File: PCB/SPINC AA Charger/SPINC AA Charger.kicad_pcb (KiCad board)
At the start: 4 copper layers, 70 x 72 mm, 84 parts, among them J1 USB_C_Receptacle_USB2.0, J2 Conn_01x03_Pin, J3 Conn_01x10_Socket, J4 Conn_01x01_Pin, J5 Conn_01x01_Pin, Q1 DMG2301L, Q2 DMHC3025LSD, Q3 DMG2301L, Q4 DMG2301L, Q5 SI2305CDS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

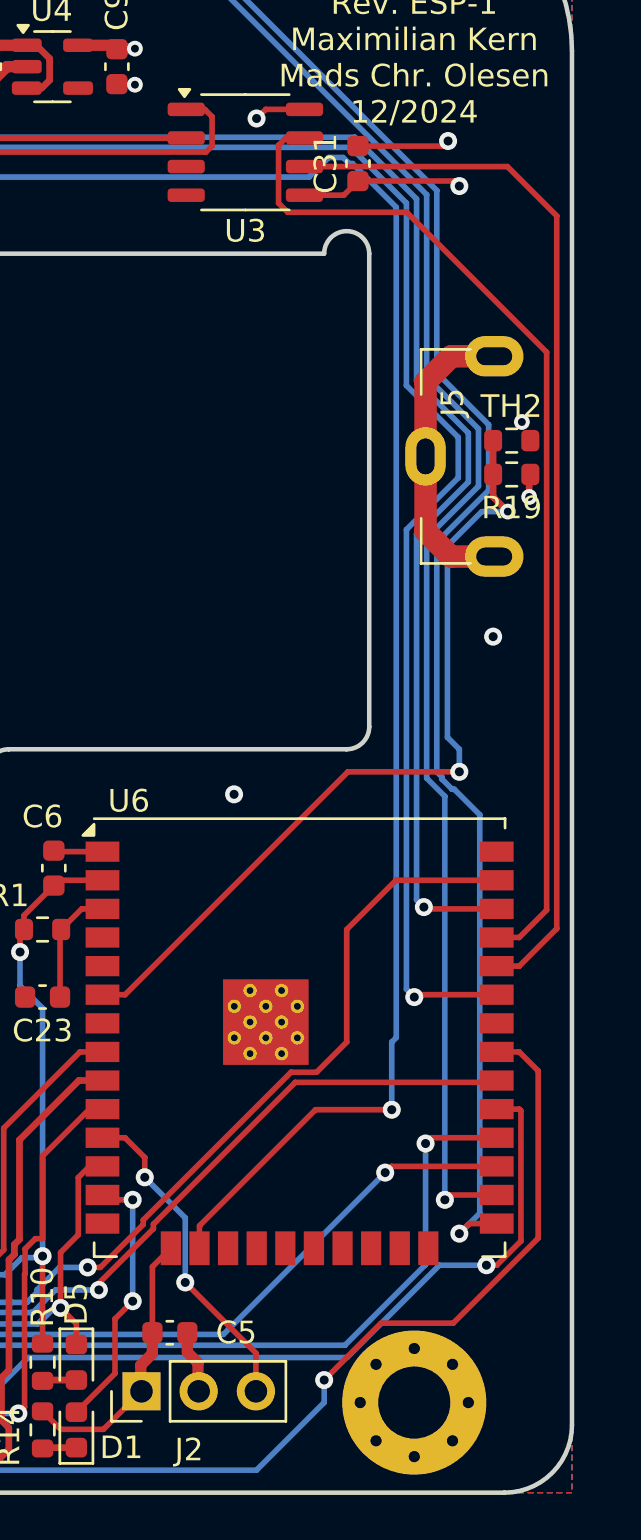
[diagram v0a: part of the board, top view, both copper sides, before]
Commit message: Fix a few routing warnings
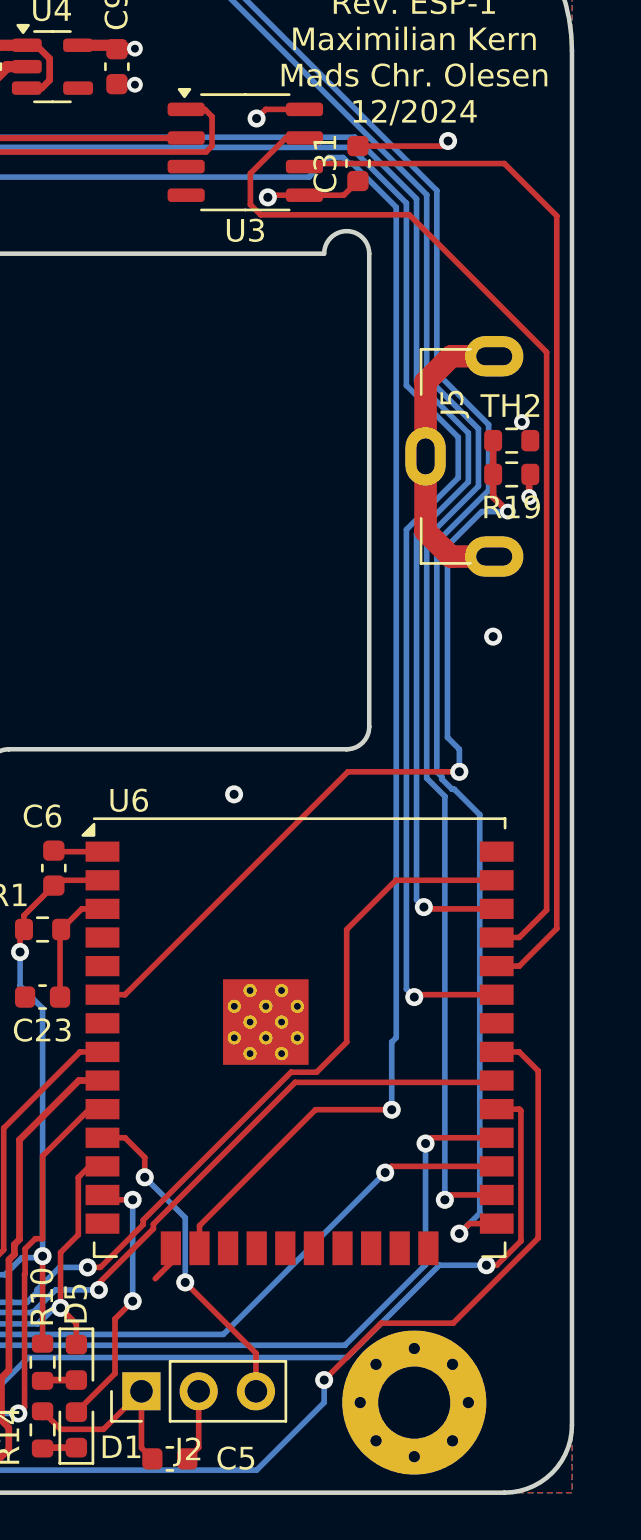
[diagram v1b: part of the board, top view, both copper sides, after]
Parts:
- moved C5 5.60 mm to (167.2, 134.5)
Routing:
- net GND: track 38.5 -> 36.4 mm
- net TX: track 46.0 -> 47.8 mm
- net +3V3: track 9.66 -> 10.4 mm
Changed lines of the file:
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@@
 	(title_block
 		(title "SPINC AA Charger")
-		(date "2024-09-29")
-		(rev "2")
-		(company "Maximilian Kern")
+		(date "2024-12-14")
+		(rev "ESP-1")
+		(company "Maximilian Kern, Mads Chr. Olesen")
 	)
 	(layers
@@
 	(footprint "Capacitor_SMD:C_0603_1608Metric"
 		(layer "F.Cu")
-		(at 167.15 128.9 180)
+		(at 167.15 134.5 180)
 		(descr "Capacitor SMD 0603 (1608 Metric), square (rectangular) end terminal, IPC_7351 nominal, (Body size source: IPC-SM-782 page 76, https://www.pcb-3d.com/wordpress/wp-content/uploads/ipc-sm-782a_amendment_1_and_2.pdf), generated with kicad-footprint-generator")
 		(tags "capacitor")
@@
 	)
 	(segment
-		(start 166.375 128.9)
-		(end 166.375 125.97)
-		(width 0.25)
-		(layer "F.Cu")
-		(net 5)
-	)
-	(segment
-		(start 166.375 129)
-		(end 166.375 129.825)
-		(width 0.5)
-		(layer "F.Cu")
-		(net 5)
-	)
-	(segment
-		(start 165.86 130.34)
-		(end 165.86 131.6)
-		(width 0.5)
-		(layer "F.Cu")
-		(net 5)
-	)
-	(segment
 		(start 179.275 76.225)
 		(end 179.5 76)
@@
 	)
 	(segment
+		(start 165.89 134.015)
+		(end 166.375 134.5)
+		(width 0.25)
+		(layer "F.Cu")
+		(net 5)
+	)
+	(segment
 		(start 161.5 132.3875)
 		(end 162.3 133.1875)
@@
 	)
 	(segment
-		(start 166.375 125.97)
-		(end 167.195 125.15)
-		(width 0.25)
-		(layer "F.Cu")
-		(net 5)
-	)
-	(segment
-		(start 166.375 129.825)
-		(end 165.86 130.34)
-		(width 0.5)
-		(layer "F.Cu")
-		(net 5)
-	)
-	(segment
 		(start 148.75 69.91)
 		(end 149.46 69.2)
@@
 	)
 	(segment
+		(start 167.195 125.15)
+		(end 167.195 125.805)
+		(width 0.25)
+		(layer "F.Cu")
+		(net 5)
+	)
+	(segment
 		(start 149.46 69.2)
 		(end 151.04 69.2)
@@
 	)
 	(segment
+		(start 165.89 131.5)
+		(end 165.89 134.015)
+		(width 0.25)
+		(layer "F.Cu")
+		(net 5)
+	)
+	(segment
 		(start 150.4 73.475)
 		(end 150.4 74.045405)
@@
 	)
 	(segment
+		(start 167.195 125.805)
+		(end 166.5 126.5)
+		(width 0.25)
+		(layer "F.Cu")
+		(net 5)
+	)
+	(segment
 		(start 175.5 76.225)
 		(end 179.275 76.225)
@@
 	)
 	(segment
+		(start 168.43 131.5)
+		(end 168.43 133.995)
+		(width 0.25)
+		(layer "F.Cu")
+		(net 24)
+	)
+	(segment
 		(start 161.8125 73.299999)
 		(end 161.8125 72.338738)
@@
 	)
 	(segment
+		(start 168.43 133.995)
+		(end 167.925 134.5)
+		(width 0.25)
+		(layer "F.Cu")
+		(net 24)
+	)
+	(segment
 		(start 142.9 69.4125)
 		(end 139.6 69.4125)
@@
 	)
 	(segment
-		(start 167.925 129.7625)
-		(end 168.4 130.2375)
-		(width 0.5)
-		(layer "F.Cu")
-		(net 24)
-	)
-	(segment
 		(start 133.7 69.4125)
 		(end 127.3875 69.4125)
@@
 	)
 	(segment
-		(start 167.925 129)
-		(end 167.925 129.7625)
-		(width 0.5)
-		(layer "F.Cu")
-		(net 24)
-	)
-	(segment
 		(start 161.223762 71.75)
 		(end 160.8 71.75)
@@
 	)
 	(segment
-		(start 168.4 130.2375)
-		(end 168.4 131.6)
-		(width 0.5)
-		(layer "F.Cu")
-		(net 24)
-	)
-	(segment
 		(start 126.2075 72.94)
 		(end 126.2075 71.9075)
@@
 	)
 	(segment
-		(start 175.5 77.775)
-		(end 179.775 77.775)
+		(start 171.595 78.405)
+		(end 171.5 78.5)
 		(width 0.25)
 		(layer "F.Cu")
@@
 	)
 	(segment
-		(start 171.405 74.595)
-		(end 171 75)
+		(start 173.125 78.405)
+		(end 171.595 78.405)
 		(width 0.25)
 		(layer "F.Cu")
@@
 	)
 	(segment
-		(start 173.22 78.5)
-		(end 173.125 78.405)
+		(start 171.405 74.595)
+		(end 171 75)
 		(width 0.25)
 		(layer "F.Cu")
@@
 	)
 	(segment
-		(start 179.775 77.775)
-		(end 180 78)
+		(start 173.22 78.5)
+		(end 173.125 78.405)
 		(width 0.25)
 		(layer "F.Cu")
@@
 	)
 	(via
-		(at 180 78)
+		(at 171.5 78.5)
 		(size 0.8)
 		(drill 0.4)
@@
 	)
 	(segment
-		(start 171.975 78.755908)
-		(end 172.381031 79.161939)
+		(start 171 78)
+		(end 171.5 78.5)
 		(width 0.25)
-		(layer "F.Cu")
-		(net 76)
+		(layer "In2.Cu")
+		(net 74)
 	)
 	(segment
-		(start 172.381031 79.161939)
-		(end 177.661939 79.161939)
+		(start 171 75)
+		(end 171 78)
+		(width 0.25)
+		(layer "In2.Cu")
+		(net 74)
+	)
+	(segment
+		(start 182.66 111.355)
+		(end 181.66 111.355)
 		(width 0.25)
 		(layer "F.Cu")
@@
 	)
 	(segment
-		(start 172.300001 75.865)
-		(end 171.975 76.190001)
+		(start 183.875 85.375)
+		(end 183.875 110.14)
 		(width 0.25)
 		(layer "F.Cu")
@@
 	)
 	(segment
-		(start 182.66 111.355)
-		(end 181.66 111.355)
+		(start 171.178984 79.275)
+		(end 177.775 79.275)
 		(width 0.25)
 		(layer "F.Cu")
@@
 	)
 	(segment
-		(start 183.875 85.375)
-		(end 183.875 110.14)
+		(start 172.300001 75.865)
+		(end 170.725 77.440001)
 		(width 0.25)
 		(layer "F.Cu")
@@
 	)
 	(segment
-		(start 171.975 76.190001)
-		(end 171.975 78.755908)
+		(start 177.775 79.275)
+		(end 183.875 85.375)
 		(width 0.25)
 		(layer "F.Cu")
@@
 	)
 	(segment
-		(start 177.661939 79.161939)
-		(end 183.875 85.375)
+		(start 170.725 78.821016)
+		(end 171.178984 79.275)
 		(width 0.25)
 		(layer "F.Cu")
@@
 	)
 	(segment
-		(start 184.325 79.325)
-		(end 184.325 110.96)
+		(start 170.725 77.440001)
+		(end 170.725 78.821016)
+		(width 0.25)
+		(layer "F.Cu")
+		(net 76)
+	)
+	(segment
+		(start 173.26 77)
+		(end 182 77)
 		(width 0.25)
 		(layer "F.Cu")
@@
 	)
 	(segment
-		(start 184.325 110.96)
-		(end 182.66 112.625)
+		(start 182 77)
+		(end 184.325 79.325)
 		(width 0.25)
 		(layer "F.Cu")
@@
 	)
 	(segment
-		(start 182.66 112.625)
-		(end 181.66 112.625)
+		(start 184.325 79.325)
+		(end 184.325 110.96)
 		(width 0.25)
 		(layer "F.Cu")
@@
 	)
 	(segment
-		(start 182.135 77.135)
-		(end 184.325 79.325)
+		(start 184.325 110.96)
+		(end 182.66 112.625)
 		(width 0.25)
 		(layer "F.Cu")
@@
 	(segment
 		(start 173.125 77.135)
-		(end 182.135 77.135)
+		(end 173.26 77)
+		(width 0.25)
+		(layer "F.Cu")
+		(net 77)
+	)
+	(segment
+		(start 182.66 112.625)
+		(end 181.66 112.625)
 		(width 0.25)
 		(layer "F.Cu")

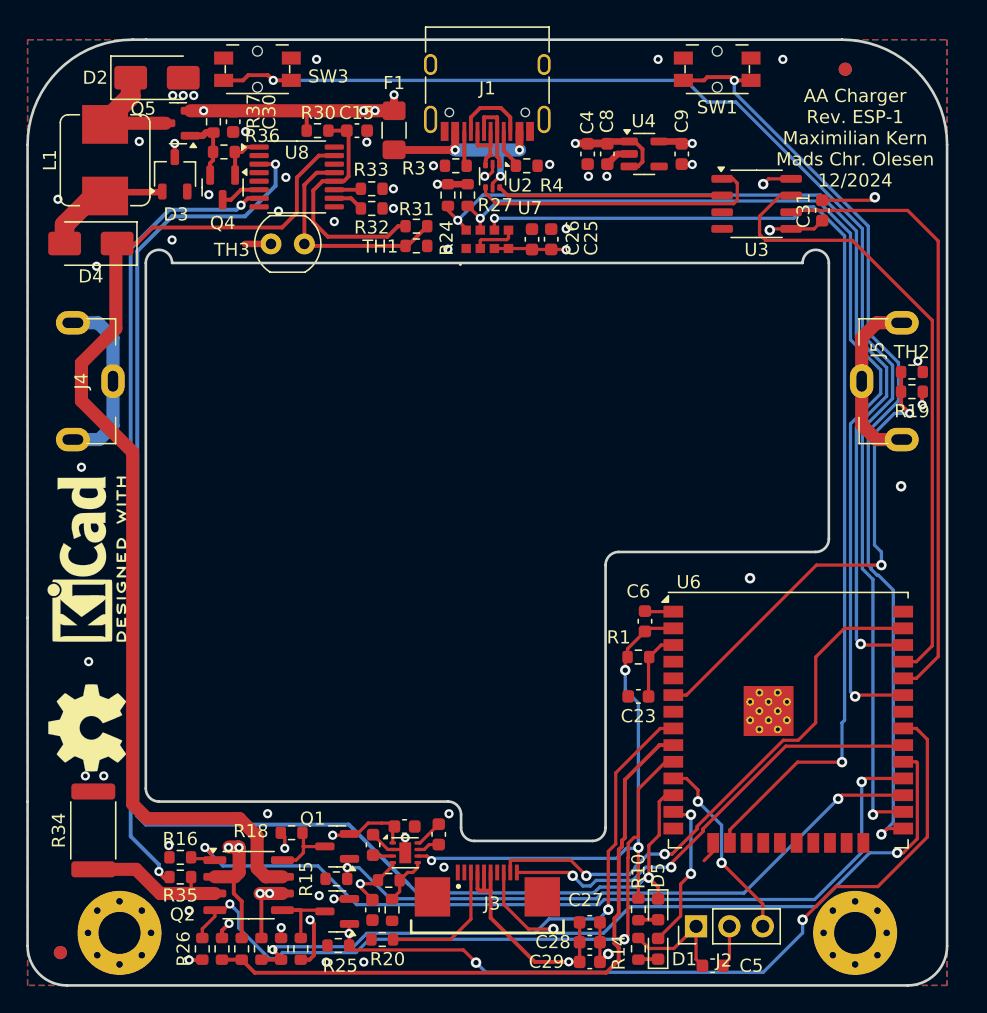
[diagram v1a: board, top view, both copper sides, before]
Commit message: Optimize PCB some more around ESP32
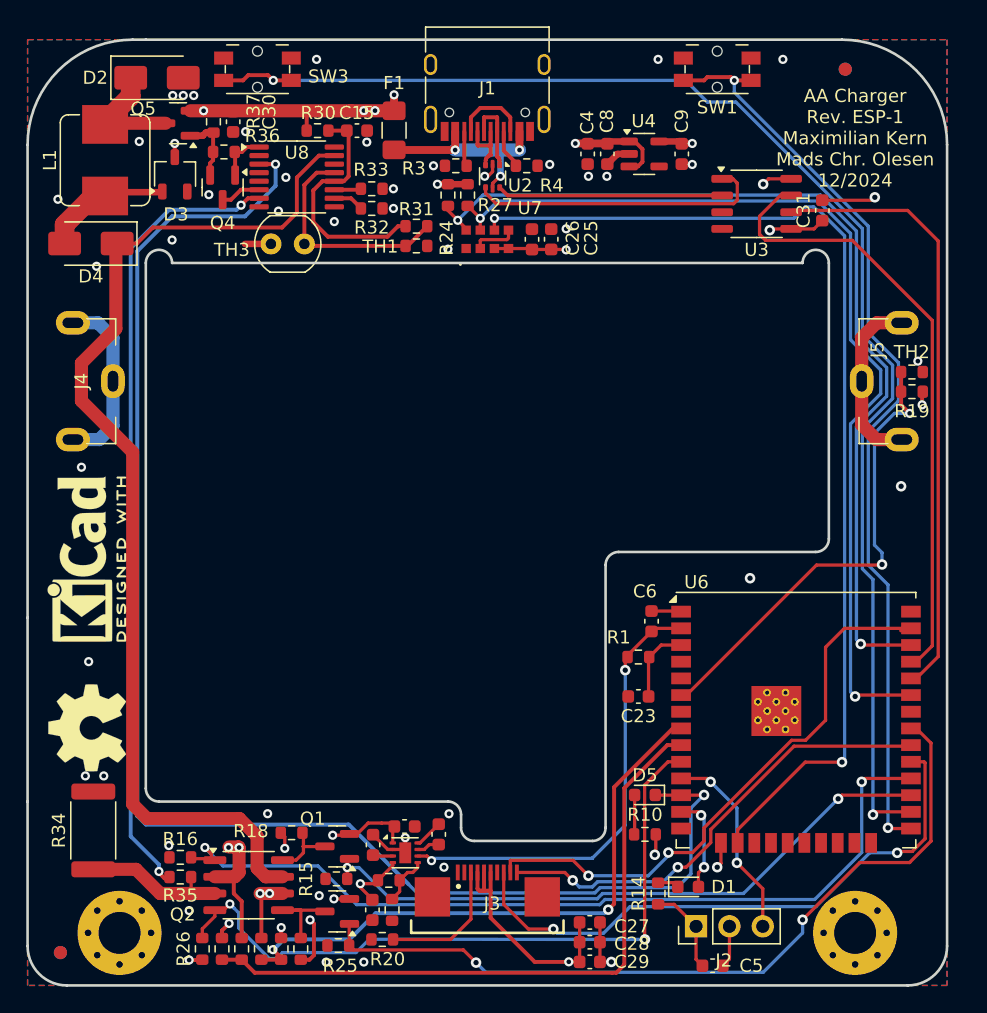
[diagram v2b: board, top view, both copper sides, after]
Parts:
- moved D5 8.77 mm to (162.0, 121.5), turned to 180 degrees
- moved R10 5.73 mm to (162.0, 124.5), turned to 180 degrees
- moved D1 5.24 mm to (165.3, 128.5), turned to 0 degrees
- moved R14 4.47 mm to (163.0, 129.0), turned to 90 degrees
- moved U6 0.59 mm to (173.5, 115.8)
- moved C6 0.50 mm to (162.5, 108.3)
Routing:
- net +3.3V: track 62.3 -> 57.8 mm
- net Net-(D1-A): track 11.9 -> 7.66 mm
- net CHG_STAT: track 110.8 -> 113.8 mm
- net LCD_CS: track 44.7 -> 46.5 mm
- net SW_1: track 72.3 -> 70.6 mm
- net Net-(D5-A): track 1.52 -> 3.02 mm
- net GND: track 36.4 -> 35.0 mm, vias 45 -> 46
- net PWM_SERVO: track 14.7 -> 16.0 mm
- net HBR_BL: track 52.9 -> 54.2 mm
- net LCD_SCK: track 34.6 -> 35.6 mm
- net LCD_MOSI: track 42.5 -> 43.3 mm
- net VCN_INT: track 80.4 -> 79.9 mm
- net HBR_BH: track 61.4 -> 61.6 mm, vias 3 -> 2

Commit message: Re-arrange a bit and reduce the number of vias.
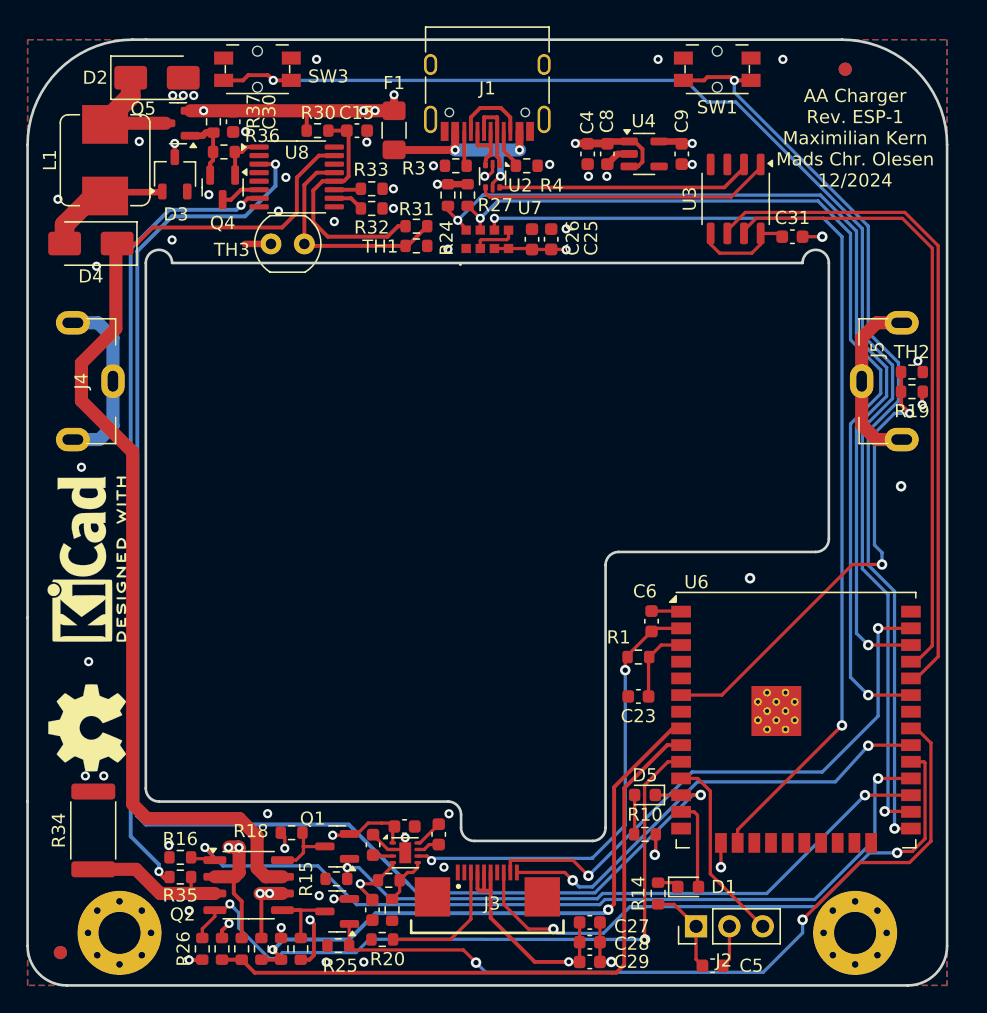
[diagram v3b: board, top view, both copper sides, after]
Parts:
- moved C31 3.03 mm to (173.2, 79.0), turned to 0 degrees
- moved U3 1.64 mm to (168.9, 76.1), turned to -90 degrees
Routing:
- net RX: track 47.2 -> 52.8 mm
- net CHG_STAT: track 113.8 -> 110.4 mm
- net GND: track 35.0 -> 32.3 mm
- net VCN_INT: track 79.9 -> 77.2 mm
- net +3V3: track 10.4 -> 7.76 mm, vias 2 -> 0
- net USB_D_N: track 17.2 -> 19.5 mm
- net TX: track 47.8 -> 49.1 mm
- net SDA: track 73.0 -> 72.3 mm
- net HBR_AH: track 48.2 -> 48.8 mm
- net Net-(D1-A): track 7.66 -> 7.20 mm, vias 2 -> 0
- net PWM_SERVO: track 16.0 -> 15.6 mm, vias 2 -> 0

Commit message: Fixup a few PCB warnings, give credit
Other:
- board text added: "AA Charger Rev. ESP-1 Maximilian Kern mchro, duck 12/2024"
- board text removed: "AA Charger Rev. ESP-1 Maximilian Kern Mads Chr. Olesen 12/2024"
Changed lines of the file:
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@@
 		(tags "capacitor")
 		(property "Reference" "C31"
-			(at 0 -1.43 360)
+			(at 0 -1.43 0)
 			(layer "F.SilkS")
 			(effects
@@
 		)
 		(property "Value" "100nF"
-			(at 0 1.43 360)
+			(at 0 1.43 0)
 			(layer "F.Fab")
 			(effects
@@
 		)
 		(fp_text user "${REFERENCE}"
-			(at 0 0 360)
+			(at 0 0 0)
 			(layer "F.Fab")
 			(effects
@@
 		(tags "Through hole pin header THT 1x03 2.54mm single row")
 		(property "Reference" "J2"
-			(at -2.6 2.11 180)
+			(at -2.25 4.61 180)
 			(layer "F.SilkS")
 			(effects
@@
 		(tags "capacitor")
 		(property "Reference" "C5"
-			(at -2.95 0 0)
+			(at 2.65 0 0)
 			(layer "F.SilkS")
 			(effects
@@
 		(layer "Edge.Cuts")
 	)
-	(gr_text "AA Charger \nRev. ESP-1\nMaximilian Kern\nMads Chr. Olesen\n12/2024"
-		(at 178 71.5 0)
+	(gr_text "AA Charger \nRev. ESP-1\nMaximilian Kern\nmchro, duck\n12/2024"
+		(at 178.25 71.5 0)
 		(layer "F.SilkS")
 		(effects

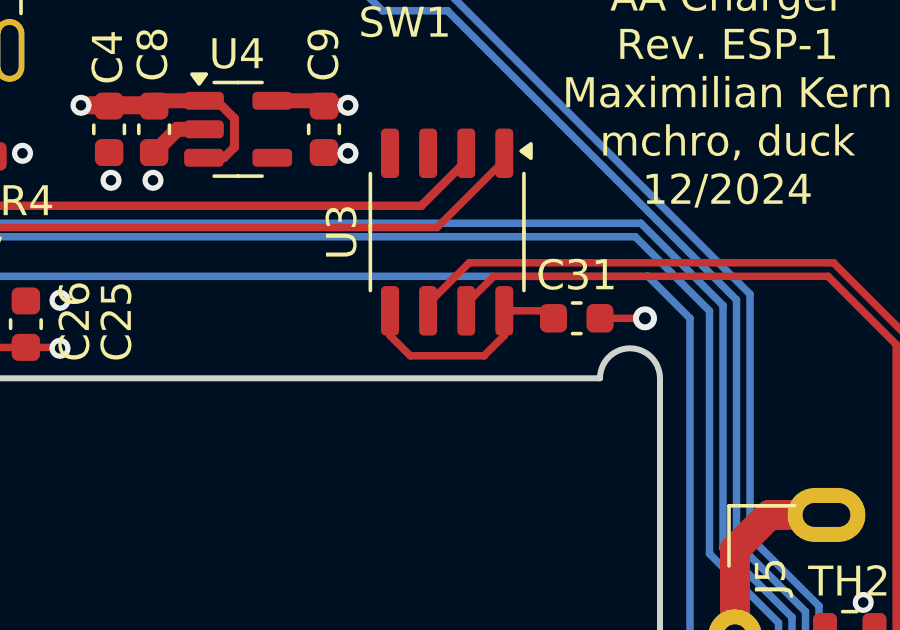
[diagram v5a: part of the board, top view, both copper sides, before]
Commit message: Fix 3V3 supply for CH340; move capacitor to supply pin
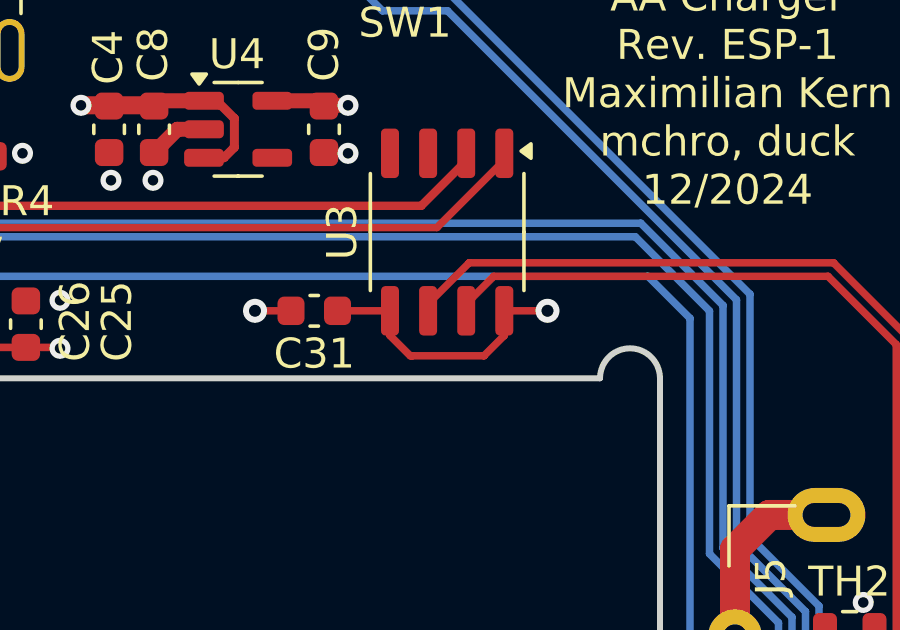
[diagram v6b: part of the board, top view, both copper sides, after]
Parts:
- moved C31 8.75 mm to (164.5, 78.8), turned to 180 degrees
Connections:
- C31 pad 1: +3V3 -> +3.3V
- U3 pad 5: +3V3 -> +3.3V
- U3 pad 8: +3V3 -> +3.3V
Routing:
- net +3.3V: track 57.8 -> 67.0 mm, vias 11 -> 12
- net +3V3: track 7.76 -> 0.00 mm
